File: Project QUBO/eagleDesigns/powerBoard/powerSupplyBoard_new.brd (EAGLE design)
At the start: 152.4 x 101.6 mm, 143 parts

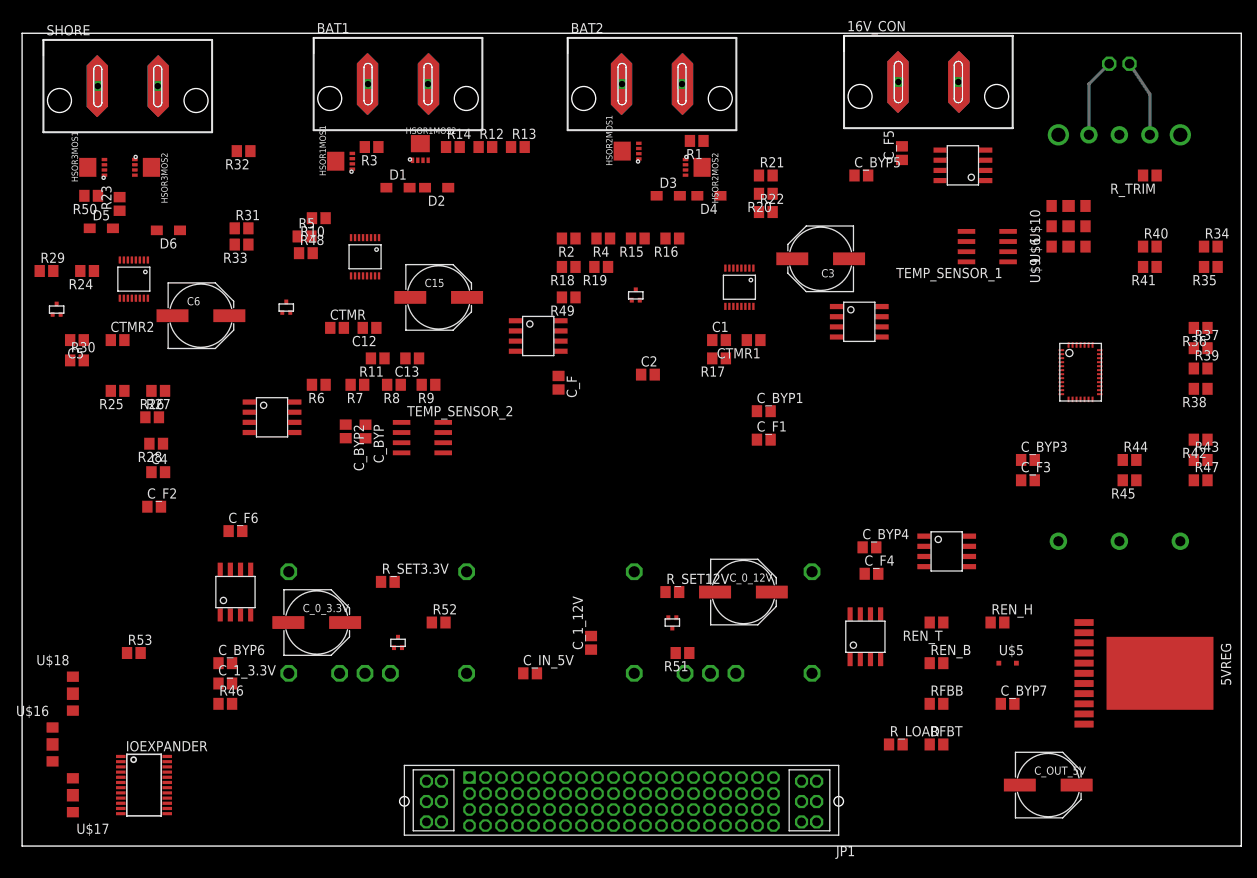
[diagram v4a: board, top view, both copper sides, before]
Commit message: 
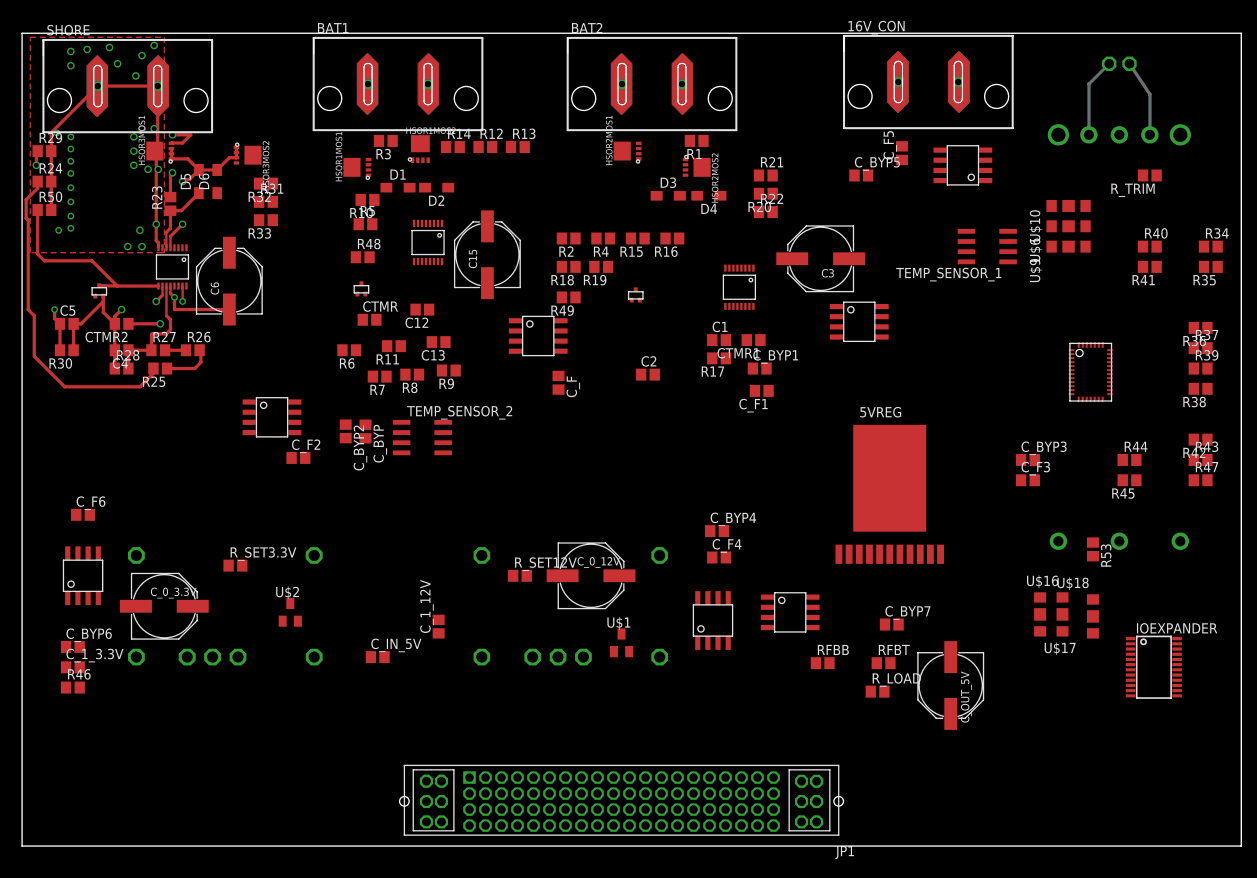
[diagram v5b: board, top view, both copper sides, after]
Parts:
- removed R51, R52: 100 kO, resistor:R0805
- removed REN_B: 12.7 kO, resistor:R0805
- removed REN_H: 10 O, resistor:R0805
- removed REN_T: 113 kO, resistor:R0805
- removed U$14, U$15: 2SK3019SOT416/SC75, transistor-fet:SOT416
- removed U$5: MMSZ5231BSSOD323-REFLOW, diode:SOD323-R
- added U$1, U$2: BSS138CT-NDSOT23, transistor-fet:SOT23
- moved U$18 127.9 mm to (133.9, 28.7)
- moved U$16 127.3 mm to (130.0, 29.0)
- moved IOEXPANDER 127.1 mm to (141.5, 22.4)
- moved U$17 123.0 mm to (127.3, 29.0)
- moved R53 120.6 mm to (133.9, 37.1), turned to 270 degrees
- moved 5VREG 41.7 mm to (108.5, 46.0), turned to 0 degrees
- moved 5VCS 21.0 mm to (96.0, 29.2)
- moved C_BYP4 19.2 mm to (86.9, 39.4)
- moved 3.3VREG 19.2 mm to (25.4, 30.0)
- moved C_1_12V 19.2 mm to (52.1, 27.4)
- moved R_SET12V 19.2 mm to (62.2, 33.8)
- moved 3.3VCS 19.2 mm to (7.62, 33.8)
- moved C_F6 19.2 mm to (7.62, 41.4)
- moved 12VCS 19.2 mm to (86.4, 28.2)
- moved 12VREG 19.2 mm to (68.6, 30.0)
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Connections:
- removed net N$58: 5VREG.EN, REN_H.2
- new net N$41: 5VREG.EN
- net 12VEN: now also U$1.1; no longer U$14.G
- net 3.3VEN: now also U$2.1; no longer U$15.G
- net AGND: now also U$1.2, U$2.2; no longer REN_B.1, REN_B.2, REN_H.1, REN_T.2, U$14.S, U$15.S, U$5.A, U$5.C
- net N$87: now also U$1.3; no longer R51.1, U$14.D
- net N$89: now also U$2.3; no longer R52.1, U$15.D
- net VIN: no longer R51.2, R52.2, REN_T.1
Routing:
- net BAT3: track 0.00 -> 45.9 mm, vias 0 -> 29
- net N$37: track 0.00 -> 42.0 mm, vias 0 -> 3
- net N$33: track 0.00 -> 40.6 mm
- net AGND: track 0.00 -> 37.2 mm, vias 0 -> 2
- net N$56: track 0.00 -> 24.5 mm
- net N$11: track 0.00 -> 23.5 mm, vias 0 -> 2
- net N$36: track 0.00 -> 15.5 mm
- net N$44: track 0.00 -> 13.0 mm, vias 0 -> 2
- net N$42: track 0.00 -> 9.86 mm, vias 0 -> 2
- net N$30: track 0.00 -> 9.31 mm
- net N$34: track 0.00 -> 6.14 mm
- net N$35: track 0.00 -> 2.62 mm
- added copper zone on layer 1, net BAT3
- added copper zone on layer 15, net BAT3
- added copper zone on layer 2, net BAT3

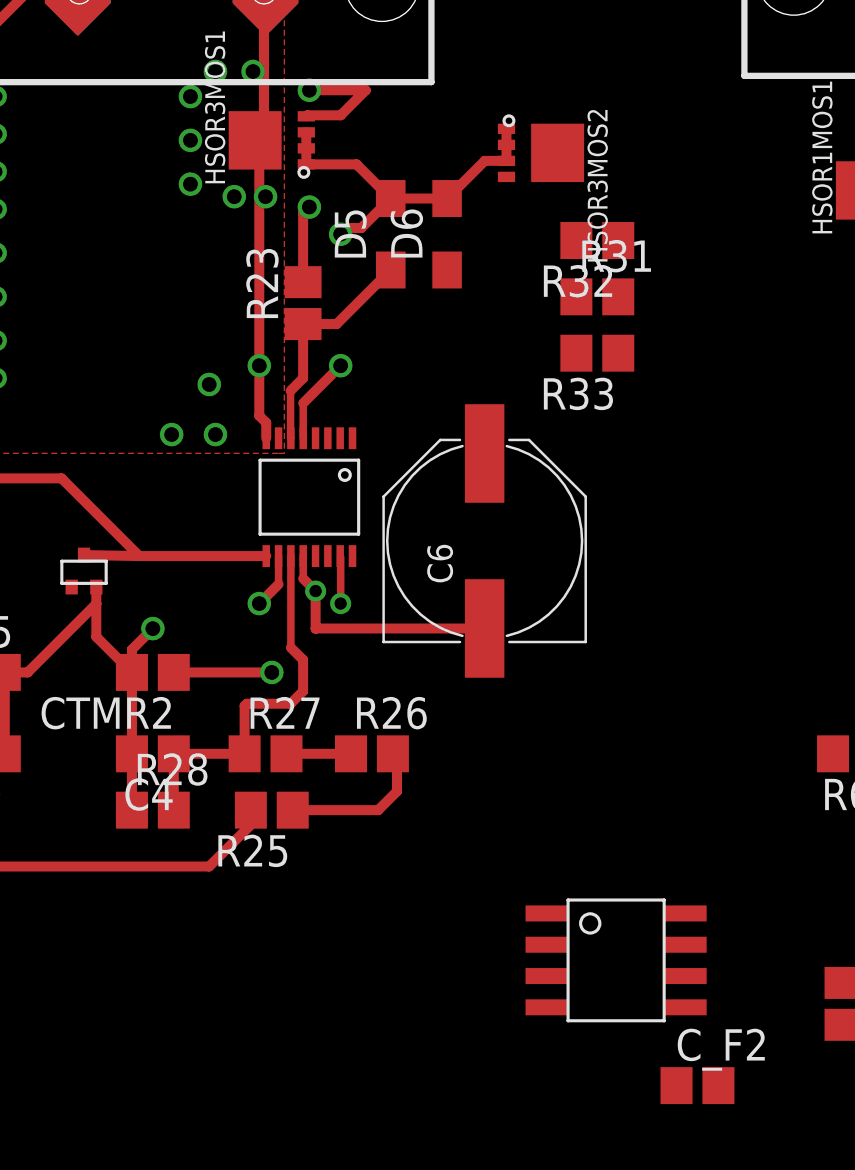
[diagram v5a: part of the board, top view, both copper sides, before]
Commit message: 
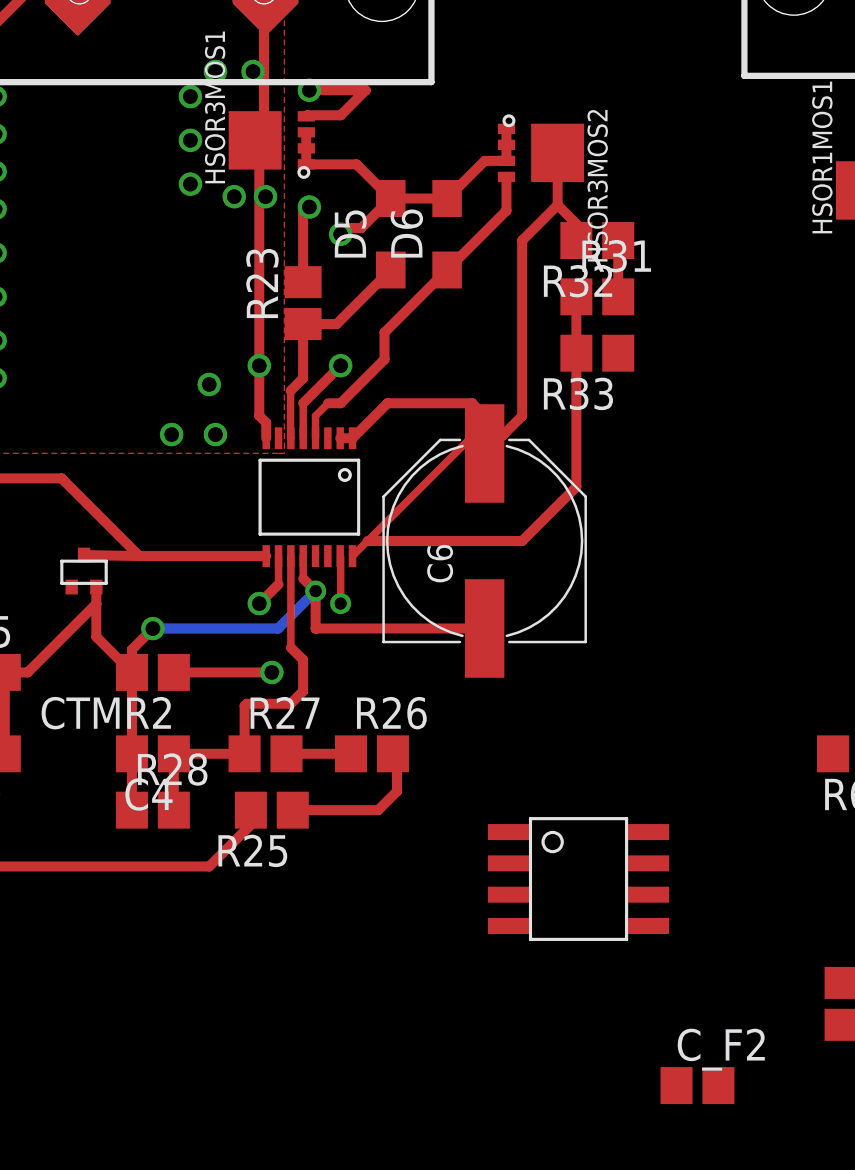
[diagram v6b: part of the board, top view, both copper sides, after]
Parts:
- moved BAT3CS 3.64 mm to (29.7, 56.9)
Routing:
- net N$40: track 0.00 -> 25.3 mm
- net BAT3HSOROUT: track 0.00 -> 22.9 mm
- net N$31: track 0.00 -> 14.1 mm
- net N$38: track 0.00 -> 2.29 mm
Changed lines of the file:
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@@
 <element name="BAT2CS" library="allegro" package="ACS713-SOIC" value="ACS713SOIC" x="104.648" y="65.532" rot="R270"/>
 <element name="BAT2HSOR" library="linear" package="MSOP16" value="LTC4364MSOP" x="89.662" y="69.85" rot="R180"/>
-<element name="BAT3CS" library="allegro" package="ACS713-SOIC" value="ACS713SOIC" x="31.242" y="53.594" rot="R270"/>
+<element name="BAT3CS" library="allegro" package="ACS713-SOIC" value="ACS713SOIC" x="29.718" y="56.896" rot="R270"/>
 <element name="BAT3HSOR" library="linear" package="MSOP16" value="LTC4364MSOP" x="18.796" y="72.39" rot="R180"/>
 <element name="C1" library="resistor" package="C0805" value="1 nF" x="87.122" y="63.246"/>
@@
 <wire x1="42.926" y1="52.666" x2="52.638" y2="52.959" width="0" layer="19" extent="1-1"/>
 <wire x1="40.45" y1="52.68" x2="42.926" y2="52.666" width="0" layer="19" extent="1-1"/>
-<wire x1="34.042" y1="55.499" x2="40.45" y2="52.68" width="0" layer="19" extent="1-1"/>
-<wire x1="5.715" y1="36.582" x2="34.042" y2="55.499" width="0" layer="19" extent="1-1"/>
+<wire x1="32.518" y1="58.801" x2="40.45" y2="52.68" width="0" layer="19" extent="1-1"/>
+<wire x1="5.715" y1="36.582" x2="32.518" y2="58.801" width="0" layer="19" extent="1-1"/>
 <wire x1="5.5" y1="24.892" x2="5.715" y2="36.582" width="0" layer="19" extent="1-1"/>
 </signal>
@@
 <wire x1="23.8125" y1="23.622" x2="43.6" y2="23.622" width="0" layer="19" extent="1-1"/>
 <wire x1="5.5" y1="22.352" x2="23.8125" y2="23.622" width="0" layer="19" extent="1-1"/>
-<wire x1="28.442" y1="51.689" x2="23.8125" y2="23.622" width="0" layer="19" extent="1-1"/>
-<wire x1="28.442" y1="52.959" x2="28.442" y2="51.689" width="0" layer="19" extent="1-1"/>
-<wire x1="61.716" y1="61.849" x2="28.442" y2="52.959" width="0" layer="19" extent="1-1"/>
+<wire x1="26.918" y1="54.991" x2="23.8125" y2="23.622" width="0" layer="19" extent="1-1"/>
+<wire x1="26.918" y1="56.261" x2="26.918" y2="54.991" width="0" layer="19" extent="1-1"/>
+<wire x1="61.716" y1="61.849" x2="26.918" y2="56.261" width="0" layer="19" extent="1-1"/>
 <wire x1="61.716" y1="63.119" x2="61.716" y2="61.849" width="0" layer="19" extent="1-1"/>
 </signal>
@@
 <contactref element="D6" pad="C"/>
 <contactref element="HSOR3MOS2" pad="GATE"/>
-<wire x1="24.384" y1="81.608" x2="26.794" y2="85.385" width="0" layer="19" extent="1-1"/>
-<wire x1="19.046" y1="74.78" x2="24.384" y2="81.608" width="0" layer="19" extent="1-1"/>
+<wire x1="26.794" y1="84.018" x2="24.384" y2="81.608" width="0.4064" layer="1"/>
+<wire x1="26.794" y1="84.018" x2="26.794" y2="85.385" width="0.4064" layer="1"/>
+<wire x1="24.384" y1="81.608" x2="21.844" y2="79.068" width="0.4064" layer="1"/>
+<wire x1="21.844" y1="79.068" x2="21.844" y2="77.978" width="0.4064" layer="1"/>
+<wire x1="21.844" y1="77.978" x2="20.066" y2="76.2" width="0.4064" layer="1"/>
+<wire x1="20.066" y1="76.2" x2="19.558" y2="76.2" width="0.4064" layer="1"/>
+<wire x1="19.558" y1="76.2" x2="19.046" y2="75.688" width="0.3048" layer="1"/>
+<wire x1="19.046" y1="75.688" x2="19.046" y2="74.78" width="0.3048" layer="1"/>
 </signal>
 <signal name="N$33">
@@
 <contactref element="R31" pad="2"/>
 <contactref element="R32" pad="1"/>
-<wire x1="31.33" y1="80.518" x2="31.33" y2="82.804" width="0" layer="19" extent="1-1"/>
+<wire x1="31.33" y1="80.518" x2="31.33" y2="82.804" width="0.4064" layer="1"/>
 </signal>
 <signal name="N$40">
@@
 <contactref element="R31" pad="1"/>
 <contactref element="BAT3HSOR" pad="FB"/>
-<wire x1="29.63" y1="78.232" x2="29.63" y2="80.518" width="0" layer="19" extent="1-1"/>
-<wire x1="20.546" y1="70" x2="29.63" y2="78.232" width="0" layer="19" extent="1-1"/>
+<wire x1="29.63" y1="78.232" x2="29.63" y2="80.518" width="0.4064" layer="1"/>
+<wire x1="21.158" y1="70.612" x2="20.546" y2="70" width="0.3048" layer="1"/>
+<wire x1="21.158" y1="70.612" x2="27.432" y2="70.612" width="0.4064" layer="1"/>
+<wire x1="27.432" y1="70.612" x2="29.63" y2="72.81" width="0.4064" layer="1"/>
+<wire x1="29.63" y1="72.81" x2="29.63" y2="78.232" width="0.4064" layer="1"/>
+<wire x1="21.158" y1="70.612" x2="25.4" y2="74.854" width="0.3048" layer="1"/>
+<wire x1="25.4" y1="74.854" x2="25.4" y2="76.2" width="0.4064" layer="1"/>
 </signal>
 <signal name="BAT3HSOROUT">
@@
 <contactref element="BAT3HSOR" pad="SENSE"/>
 <contactref element="HSOR3MOS2" pad="DRAIN"/>
-<wire x1="29.63" y1="82.804" x2="28.869" y2="86.36" width="0" layer="19" extent="1-1"/>
-<wire x1="25.908" y1="74.162" x2="29.63" y2="82.804" width="0" layer="19" extent="1-1"/>
-<wire x1="20.546" y1="74.78" x2="25.908" y2="74.162" width="0" layer="19" extent="1-1"/>
-<wire x1="20.046" y1="74.78" x2="20.546" y2="74.78" width="0" layer="19" extent="1-1"/>
-<wire x1="28.442" y1="55.499" x2="25.908" y2="74.162" width="0" layer="19" extent="1-1"/>
-<wire x1="28.442" y1="54.229" x2="28.442" y2="55.499" width="0" layer="19" extent="1-1"/>
+<wire x1="26.673" y1="74.927" x2="25.908" y2="74.162" width="0.4064" layer="1"/>
+<wire x1="26.673" y1="74.927" x2="27.432" y2="75.686" width="0.4064" layer="1"/>
+<wire x1="27.432" y1="75.686" x2="27.432" y2="82.804" width="0.4064" layer="1"/>
+<wire x1="27.432" y1="82.804" x2="28.869" y2="84.241" width="0.4064" layer="1"/>
+<wire x1="28.869" y1="84.241" x2="28.869" y2="86.36" width="0.4064" layer="1"/>
+<wire x1="28.869" y1="84.241" x2="29.63" y2="83.48" width="0.4064" layer="1"/>
+<wire x1="29.63" y1="83.48" x2="29.63" y2="82.804" width="0.4064" layer="1"/>
+<wire x1="21.966" y1="76.2" x2="20.546" y2="74.78" width="0.4064" layer="1"/>
+<wire x1="21.966" y1="76.2" x2="25.4" y2="76.2" width="0.4064" layer="1"/>
+<wire x1="25.4" y1="76.2" x2="26.673" y2="74.927" width="0.4064" layer="1"/>
+<wire x1="20.546" y1="74.78" x2="20.046" y2="74.78" width="0.4064" layer="1"/>
+<wire x1="26.918" y1="58.801" x2="25.908" y2="74.162" width="0" layer="19" extent="1-1"/>
+<wire x1="26.918" y1="57.531" x2="26.918" y2="58.801" width="0" layer="19" extent="1-1"/>
 </signal>
 <signal name="N$42">
@@
 <contactref element="BAT3CS" pad="P$6"/>
 <contactref element="C_F2" pad="1"/>
-<wire x1="33.694" y1="48.514" x2="34.042" y2="52.959" width="0" layer="19" extent="1-1"/>
+<wire x1="33.694" y1="48.514" x2="32.518" y2="56.261" width="0" layer="19" extent="1-1"/>
 </signal>
 <signal name="BAT3">
@@
 <contactref element="ADC" pad="CH2"/>
 <contactref element="BAT3CS" pad="P$7"/>
-<wire x1="34.042" y1="54.229" x2="131.18" y2="57.48" width="0" layer="19" extent="1-1"/>
+<wire x1="32.518" y1="57.531" x2="131.18" y2="57.48" width="0" layer="19" extent="1-1"/>
 </signal>
 <signal name="N$68">
@@
 <wire x1="11.596" y1="66.206" x2="12.446" y2="67.056" width="0.4064" layer="1"/>
 <via x="12.446" y="67.056" extent="1-16" drill="0.6"/>
-<wire x1="12.446" y1="67.056" x2="17.526" y2="67.056" width="0.4064" layer="15"/>
-<wire x1="17.526" y1="67.056" x2="19.05" y2="68.58" width="0.4064" layer="15"/>
+<wire x1="12.446" y1="67.056" x2="17.526" y2="67.056" width="0.4064" layer="16"/>
+<wire x1="17.526" y1="67.056" x2="19.05" y2="68.58" width="0.4064" layer="16"/>
 <via x="19.05" y="68.58" extent="1-16" drill="0.5"/>
 <wire x1="18.546" y1="69.084" x2="19.05" y2="68.58" width="0.4064" layer="1"/>
@@
 <wire x1="87.972" y1="63.246" x2="90.59" y2="63.246" width="0" layer="19" extent="1-1"/>
 <wire x1="87.972" y1="60.96" x2="87.972" y2="63.246" width="0" layer="19" extent="1-1"/>
-<wire x1="93.052" y1="59.69" x2="87.972" y2="60.96" width="0" layer="19" extent="1-1"/>
+<wire x1="93.052" y1="59.69" x2="90.59" y2="63.246" width="0" layer="19" extent="1-1"/>
 <wire x1="91.606" y1="56.896" x2="93.052" y2="59.69" width="0" layer="19" extent="1-1"/>
 <wire x1="79.082" y1="58.928" x2="87.972" y2="60.96" width="0" layer="19" extent="1-1"/>
@@
 <wire x1="40.45" y1="50.98" x2="42.926" y2="50.966" width="0" layer="19" extent="1-1"/>
 <wire x1="35.394" y1="48.514" x2="40.45" y2="50.98" width="0" layer="19" extent="1-1"/>
-<wire x1="34.042" y1="51.689" x2="35.394" y2="48.514" width="0" layer="19" extent="1-1"/>
+<wire x1="32.518" y1="54.991" x2="35.394" y2="48.514" width="0" layer="19" extent="1-1"/>
 <wire x1="36.5125" y1="36.322" x2="35.394" y2="48.514" width="0" layer="19" extent="1-1"/>
 <wire x1="34.478" y1="28.11" x2="36.5125" y2="36.322" width="0" layer="19" extent="1-1"/>
